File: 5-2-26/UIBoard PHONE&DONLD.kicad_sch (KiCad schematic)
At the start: 127 parts, among them J3 430450200, J4 430450200, J5 M22-7130442, J7 22035035, Q1 2N3904, Q2 2N3904, Q3 2N3904, Q4 2N3904, SW1 A8L-11-12N1, U1 UA78M05-Q1, U2 MCP2562-E-P, U3 CD4511BPWR, U4 UA78M05-Q1, U5 7 Segment Display, U6 STM32 Nucleo F446RE, U7 PCF8574AP

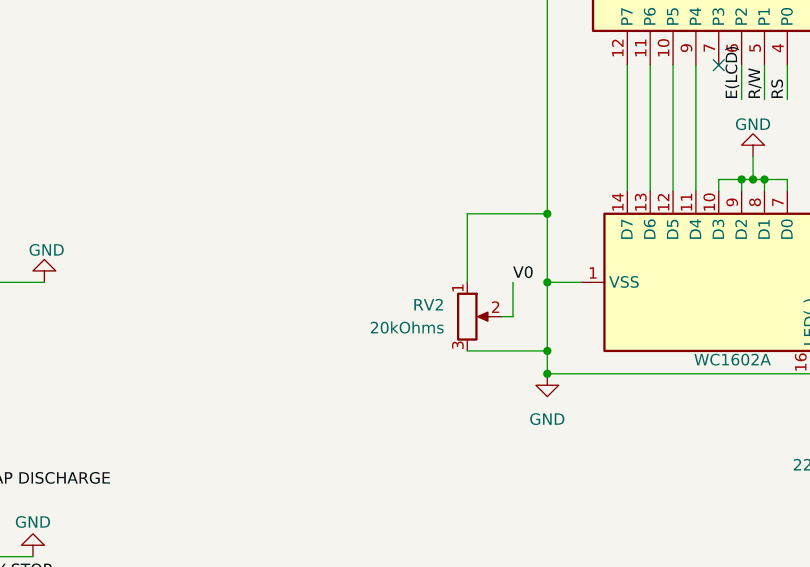
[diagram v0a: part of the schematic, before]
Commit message: changed 20k potentometer footprint
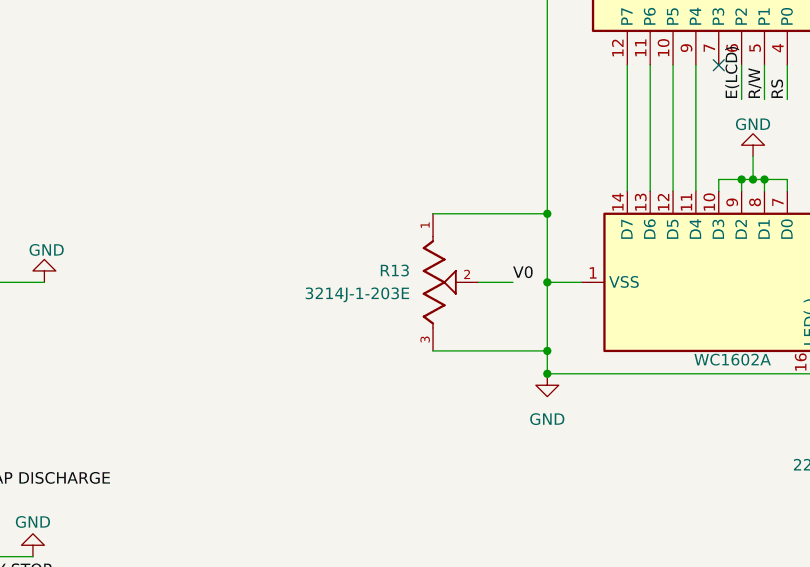
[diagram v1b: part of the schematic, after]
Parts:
- removed RV2: 20kOhms, Potentiometer_SMD:Potentiometer_ACP_CA6-VSMD_Vertical, symbol Device:R_Potentiometer
- added R13: 3214J-1-203E, SMV_ICs:TRIM_3214J-1-203E, symbol SMV_Custom:3214J-1-203E
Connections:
- net GND: now also R13.1, R13.3
- net V0: now also R13.2
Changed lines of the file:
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@@
 	(wire
 		(pts
-			(xy 236.22 101.6) (xy 236.22 93.98)
-		)
-		(stroke
-			(width 0)
-			(type default)
-		)
-	)
-	(wire
-		(pts
 			(xy 260.35 269.24) (xy 260.35 270.51)
 		)
@@
 	(wire
 		(pts
+			(xy 232.41 93.98) (xy 245.11 93.98)
+		)
+		(stroke
+			(width 0)
+			(type default)
+		)
+	)
+	(wire
+		(pts
 			(xy 21.59 62.23) (xy 24.13 62.23)
 		)
@@
 	(wire
 		(pts
-			(xy 236.22 93.98) (xy 245.11 93.98)
+			(xy 33.02 261.62) (xy 35.56 261.62)
 		)
 		(stroke
@@
 	(wire
 		(pts
-			(xy 33.02 261.62) (xy 35.56 261.62)
+			(xy 232.41 109.22) (xy 245.11 109.22)
 		)
 		(stroke
@@
 	(wire
 		(pts
-			(xy 236.22 109.22) (xy 245.11 109.22)
-		)
-		(stroke
-			(width 0)
-			(type default)
-		)
-	)
-	(wire
-		(pts
 			(xy 121.92 144.78) (xy 129.54 144.78)
 		)
@@
 	(wire
 		(pts
-			(xy 241.3 101.6) (xy 241.3 105.41)
+			(xy 354.33 107.95) (xy 363.22 107.95)
 		)
 		(stroke
@@
 	(wire
 		(pts
-			(xy 354.33 107.95) (xy 363.22 107.95)
+			(xy 237.49 101.6) (xy 241.3 101.6)
 		)
 		(stroke
@@
 	(wire
 		(pts
-			(xy 241.3 105.41) (xy 240.03 105.41)
-		)
-		(stroke
-			(width 0)
-			(type default)
-		)
-	)
-	(wire
-		(pts
 			(xy 214.63 205.74) (xy 217.17 205.74)
 		)
@@
 	)
 	(symbol
+		(lib_id "SMV_Custom:3214J-1-203E")
+		(at 232.41 101.6 270)
+		(unit 1)
+		(body_style 1)
+		(exclude_from_sim no)
+		(in_bom yes)
+		(on_board yes)
+		(in_pos_files yes)
+		(dnp no)
+		(fields_autoplaced yes)
+		(property "Reference" "R13"
+			(at 229.87 100.3299 90)
+			(show_name no)
+			(do_not_autoplace no)
+			(effects
+				(font
+					(size 1.27 1.27)
+				)
+				(justify right)
+			)
+		)
+		(property "Value" "3214J-1-203E"
+			(at 229.87 102.8699 90)
+			(show_name no)
+			(do_not_autoplace no)
+			(effects
+				(font
+					(size 1.27 1.27)
+				)
+				(justify right)
+			)
+		)
+		(property "Footprint" "SMV_ICs:TRIM_3214J-1-203E"
+			(at 232.41 101.6 0)
+			(hide yes)
+			(show_name no)
+			(do_not_autoplace no)
+			(effects
+				(font
+					(size 1.27 1.27)
+				)
+				(justify bottom)
+			)
+		)
+		(property "Datasheet" ""
+			(at 232.41 101.6 0)
+			(hide yes)
+			(show_name no)
+			(do_not_autoplace no)
+			(effects
+				(font
+					(size 1.27 1.27)
+				)
+			)
+		)
+		(property "Description" ""
+			(at 232.41 101.6 0)
+			(hide yes)
+			(show_name no)
+			(do_not_autoplace no)
+			(effects
+				(font
+					(size 1.27 1.27)
+				)
+			)
+		)
+		(property "MAXIMUM_PACKAGE_HEIGHT" "3.71mm"
+			(at 232.41 101.6 0)
+			(hide yes)
+			(show_name no)
+			(do_not_autoplace no)
+			(effects
+				(font
+					(size 1.27 1.27)
+				)
+				(justify bottom)
+			)
+		)
+		(property "CREATOR" "ANA"
+			(at 232.41 101.6 0)
+			(hide yes)
+			(show_name no)
+			(do_not_autoplace no)
+			(effects
+				(font
+					(size 1.27 1.27)
+				)
+				(justify bottom)
+			)
+		)
+		(property "STANDARD" "Manufacturer Recommendations"
+			(at 232.41 101.6 0)
+			(hide yes)
+			(show_name no)
+			(do_not_autoplace no)
+			(effects
+				(font
+					(size 1.27 1.27)
+				)
+				(justify bottom)
+			)
+		)
+		(property "PARTREV" "06/24"
+			(at 232.41 101.6 0)
+			(hide yes)
+			(show_name no)
+			(do_not_autoplace no)
+			(effects
+				(font
+					(size 1.27 1.27)
+				)
+				(justify bottom)
+			)
+		)
+		(property "VERIFIER" "NEZY"
+			(at 232.41 101.6 0)
+			(hide yes)
+			(show_name no)
+			(do_not_autoplace no)
+			(effects
+				(font
+					(size 1.27 1.27)
+				)
+				(justify bottom)
+			)
+		)
+		(property "MANUFACTURER" "Bourns"
+			(at 232.41 101.6 0)
+			(hide yes)
+			(show_name no)
+			(do_not_autoplace no)
+			(effects
+				(font
+					(size 1.27 1.27)
+				)
+				(justify bottom)
+			)
+		)
+		(pin "3"
+		)
+		(pin "2"
+		)
+		(pin "1"
+		)
+		(instances
+			(project "UIBoard PHONE&DONLD"
+				(path "/0d7d1680-c2d8-46a8-9de1-5ca794a230ab"
+					(reference "R13")
+					(unit 1)
+				)
+			)
+		)
+	)
+	(symbol
 		(lib_id "Connector:TestPoint")
 		(at 172.72 262.89 0)
@@
 					(unit 1)
 				)
-			)
-		)
-	)
-	(symbol
-		(lib_id "Device:R_Potentiometer")
-		(at 236.22 105.41 0)
-		(unit 1)
-		(body_style 1)
-		(exclude_from_sim no)
-		(in_bom yes)
-		(on_board yes)
-		(in_pos_files yes)
-		(dnp no)
-		(fields_autoplaced yes)
-		(property "Reference" "RV2"
-			(at 233.68 104.1399 0)
-			(show_name no)
-			(do_not_autoplace no)
-			(effects
-				(font
-					(size 1.27 1.27)
-				)
-				(justify right)
-			)
-		)
-		(property "Value" "20kOhms"
-			(at 233.68 106.6799 0)
-			(show_name no)
-			(do_not_autoplace no)
-			(effects
-				(font
-					(size 1.27 1.27)
-				)
-				(justify right)
-			)
-		)
-		(property "Footprint" "Potentiometer_SMD:Potentiometer_ACP_CA6-VSMD_Vertical"
-			(at 236.22 105.41 0)
-			(hide yes)
-			(show_name no)
-			(do_not_autoplace no)
-			(effects
-				(font
-					(size 1.27 1.27)
-				)
-			)
-		)
-		(property "Datasheet" ""
-			(at 236.22 105.41 0)
-			(hide yes)
-			(show_name no)
-			(do_not_autoplace no)
-			(effects
-				(font
-					(size 1.27 1.27)
-				)
-			)
-		)
-		(property "Description" "Potentiometer"
-			(at 236.22 105.41 0)
-			(hide yes)
-			(show_name no)
-			(do_not_autoplace no)
-			(effects
-				(font
-					(size 1.27 1.27)
-				)
-			)
-		)
-		(pin "1"
-		)
-		(pin "3"
-		)
-		(pin "2"
-		)
-		(instances
-			(project "UIBoard PHONE&DONLD"
-				(path "/0d7d1680-c2d8-46a8-9de1-5ca794a230ab"
-					(reference "RV2")
-					(unit 1)
-				)
